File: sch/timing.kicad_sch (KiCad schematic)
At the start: 5 parts

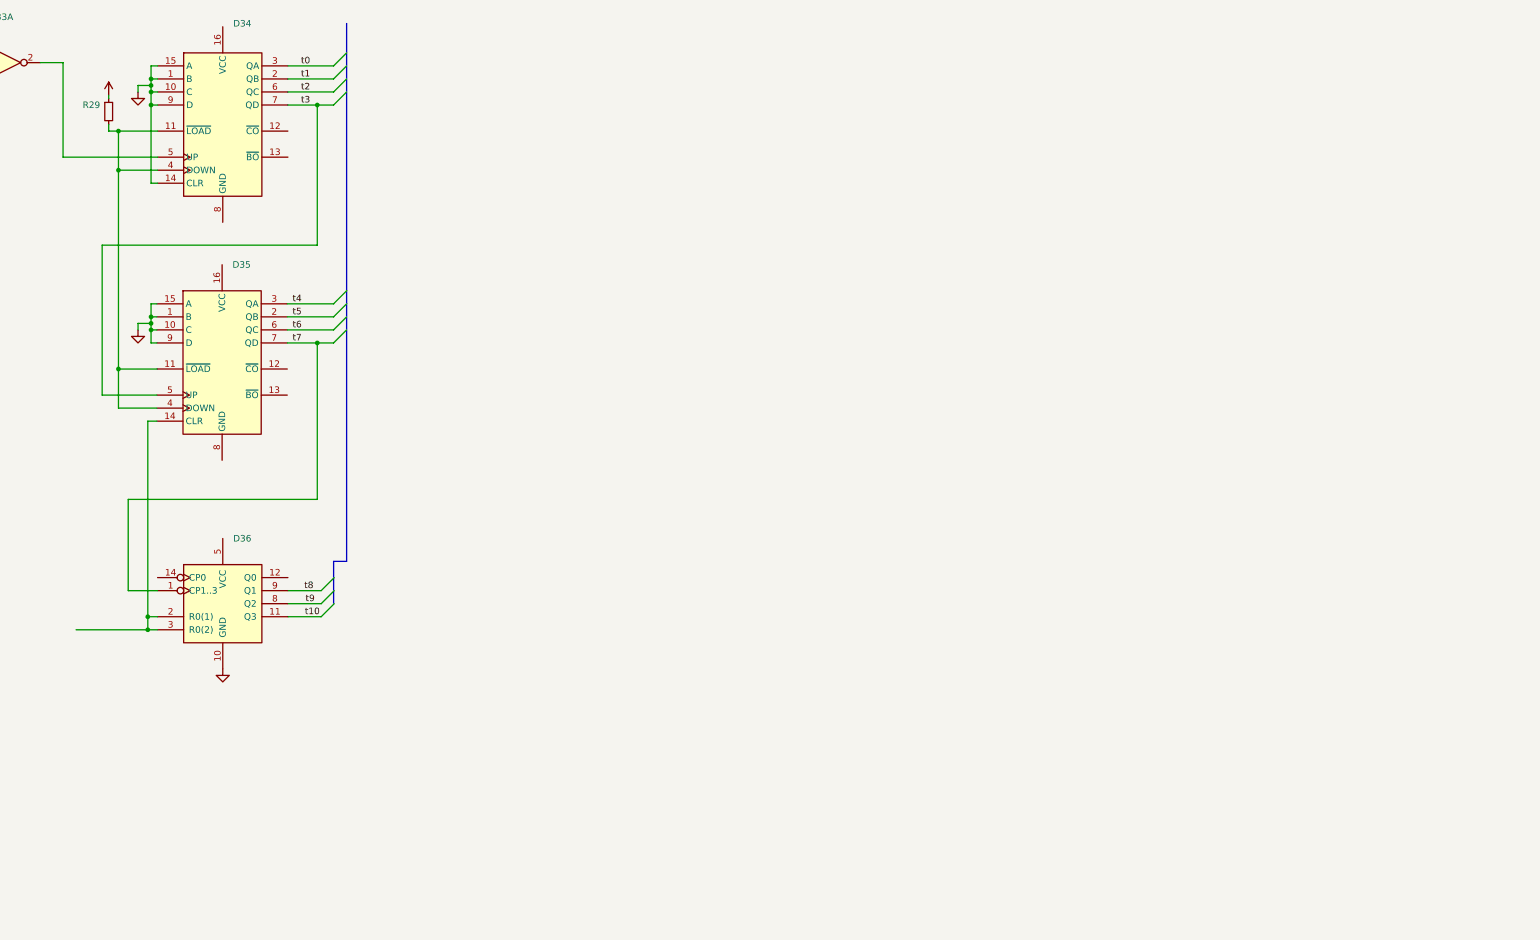
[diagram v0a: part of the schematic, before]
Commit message: Sch: timing sheet - added all elements
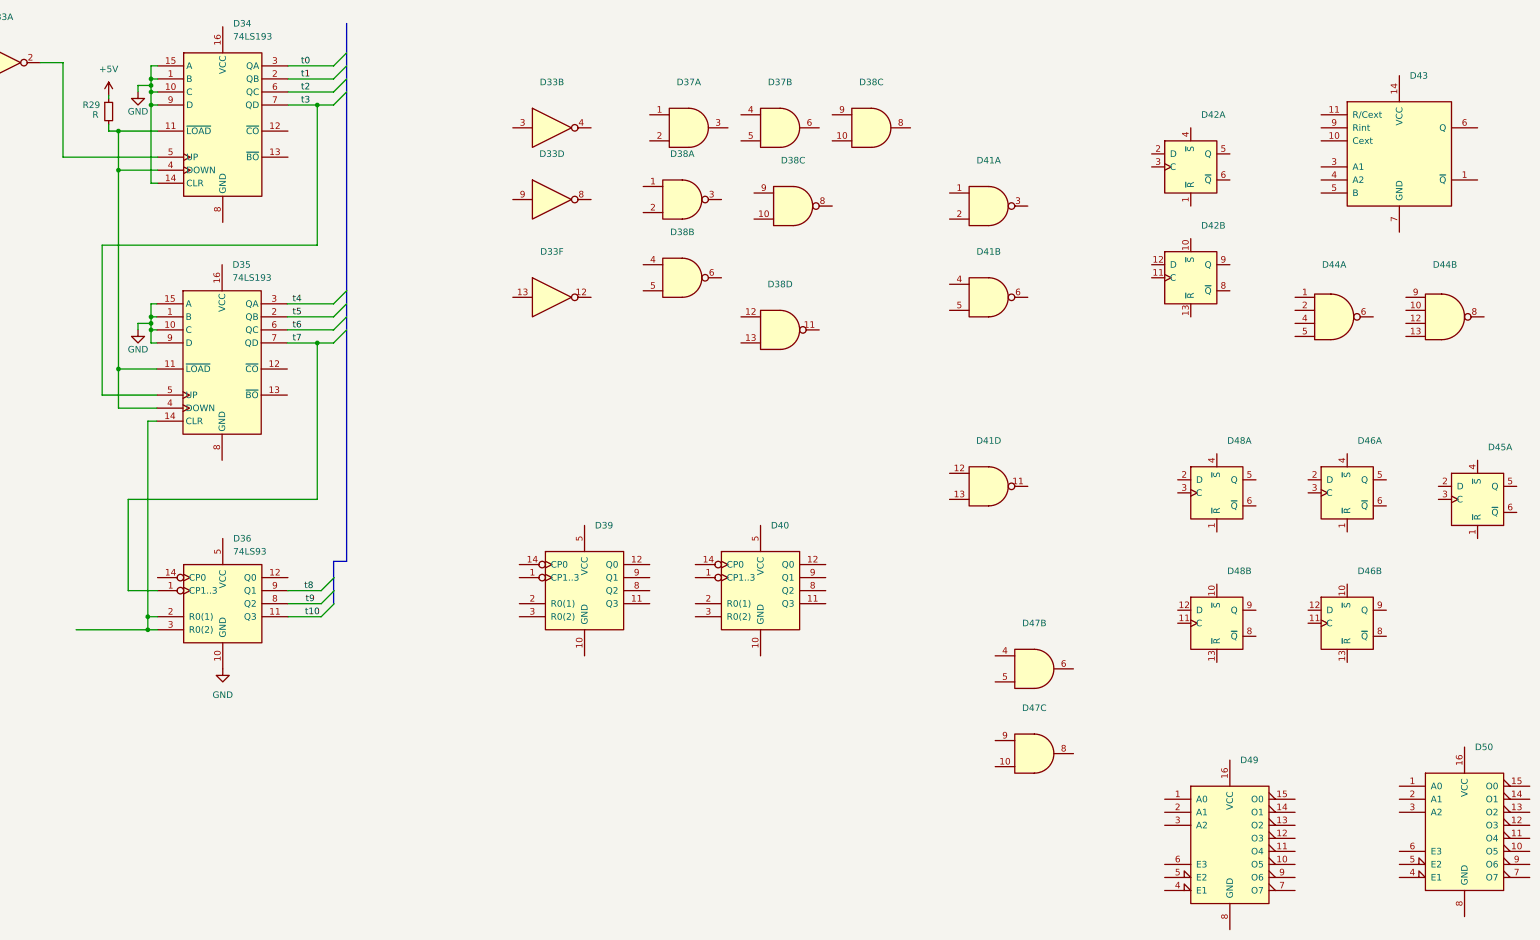
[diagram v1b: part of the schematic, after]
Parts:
- added unit 6 of D33
- added unit 2 of D33
- added unit 4 of D33
- added D37, D47: (no value), symbol 74xx:74LS08
- added D38, D41: (no value), symbol 74xx:74LS00
- added D39, D40: (no value), symbol 74xx:74LS93
- added D42, D45, D46, D48: (no value), symbol 74xx:74LS74
- added D43: (no value), symbol 74xx:74LS121
- added D44: (no value), symbol 74xx:74LS20
- added D49, D50: (no value), symbol 74xx:74LS138
- D34, D35: value (none) -> 74LS193
- D36: value (none) -> 74LS93
- R29: value (none) -> R

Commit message: SCH: timing block - work in progress
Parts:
- removed D43: (no value), symbol 74xx:74LS121
- added D1: (no value), symbol 74xx:74LS10
- added D18: (no value), symbol 74xx:74LS32
- added unit 4 of D37
- added D43: (no value), symbol 74xx:74LS123
- added R15, R16: (no value), symbol Device:R_Small
- D33: value (none) -> 74S04
- D38, D41: value (none) -> 74LS00
- D39, D40: value (none) -> 74LS93
- D42, D45, D46, D48: value (none) -> 74LS74
- D44: value (none) -> 74LS20
- D49, D50: value (none) -> 74LS138
- renumbered D38 to D37
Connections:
- net +5V: now also D49.16 (VCC), D50.16 (VCC), R15.1
- net GND: now also D46.11 (C), D46.12 (D), D46.2 (D), D46.3 (C), D48.11 (C), D48.12 (D), D48.2 (D), D48.3 (C), D49.8 (GND), D50.8 (GND)
- net t0: now also D37.4, D49.1 (A0), D50.1 (A0)
- net t1: now also D37.5, D49.2 (A1), D50.2 (A1)
- net t10: now also D37.10
- net t2: now also D49.3 (A2), D50.3 (A2)
- net t3: now also D33.3, D47.2, D50.6 (E3)
- net t6: now also D44.2
- net t7: now also D38.10, D38.9
- net t8: now also D38.1, D38.2
- net t9: now also D44.13
- net at D38.4: now also D43.4 (~{Q})
- net at D38.5: now also D45.1 (~{R}), D43.12 (~{Q})
- net CLK2: now reaches D38.6
- net CLK2: now also D35.14 (CLR), D36.2 (R0(1)), D36.3 (R0(2)), D39.14 (CP0)
- net at D41.11: now also D45.3 (C)
- net t18: now reaches D41.12
- net t18: now also D40.11 (Q3), D41.13
- net at D45.2 (D): now also D45.6 (~{Q})
- net at D45.5 (Q): now also D37.13
- net ~{KCU}: now reaches D41.4
- net ~{KCU}: now also D44.8
- net ~{CCU}: now reaches D41.5
- net ~{CCU}: now also D44.6
- net CSYNC: now reaches D41.6
- net RAM_RD_STB: now reaches D33.12
- net at D33.13: now also D50.9 (O6)
- net at D33.4: now also D37.2
- net t2??: now reaches D37.1
- net PIX_SR_LOAD: now reaches D37.3
- net at D44.10: now also D41.3
- net t15: now reaches D44.12
- net t15: now also D40.1 (CP1..3), D40.12 (Q0)
- net PIX_EN1: now reaches D44.9
- net PIX_EN1: now also D37.11, D43.9 (A)
- net at D33.8: now also D42.11 (C)
- net z5: now reaches D33.9
- net z5: now also D46.13 (~{R}), D49.9 (O6)
- net ~{RESIN}: now reaches D47.10
- net at D47.8: now also D50.4 (E1), D50.5 (E2)
- net ~{K1}: now reaches D47.9
- net ~{K1}: now also D42.8 (~{Q}), D47.1, D18.5
- net t16: now reaches D41.1
- net t16: now also D40.9 (Q1), D41.2
- net at D38.3: now also D37.9
- net z3: now reaches D48.10 (~{S})
- net z3: now also D49.12 (O3)
- net z6: now reaches D48.13 (~{R})
- net z6: now also D46.1 (~{R}), D49.7 (O7)
- net ~{CAS}: now reaches D48.8 (~{Q})
- net t14: now reaches D40.14 (CP0)
- net t14: now also D39.11 (Q3)
- net rst2: now reaches D40.2 (R0(1))
- net rst2: now also D39.2 (R0(1)), D39.3 (R0(2)), D40.3 (R0(2)), D43.5 (Q)
- net t17: now reaches D40.8 (Q2)
- net t17: now also D38.12, D38.13
- net at D42.10 (~{S}): now also D42.1 (~{R}), R16.2
- net at D42.12 (D): now also D42.6 (~{Q})
- net VIDEO-CPU: now reaches D42.13 (~{R})
- net VIDEO-CPU: now also D42.4 (~{S}), D50.7 (O7)
- net K1: now reaches D42.9 (Q)
- net at D49.10 (O5): now also D48.1 (~{R})
- net z2: now reaches D49.13 (O2)
- net z2: now also D46.4 (~{S}), D48.4 (~{S})
- net z1: now reaches D49.14 (O1)
- net z1: now also D46.10 (~{S})
- net at D49.4 (E1): now also D47.3, D49.5 (E2)
- net at D49.6 (E3): now also R15.2
- net at D38.8: now also D44.4, D44.5
- net at D38.11: now also D37.12
- net 0_ROMSEL: now reaches D42.2 (D)
- net at D42.3 (C): now also D1.8
- net ~{RAS}: now reaches D46.8 (~{Q})
- net PIX_SR_CLK: now reaches D37.6
- net K0: now reaches D46.5 (Q)
- net t11: now reaches D39.1 (CP1..3)
- net t11: now also D39.12 (Q0)
- net t13: now reaches D39.8 (Q2)
- net t12: now reaches D39.9 (Q1)
- net at D37.8: now also D43.1 (A)
- new net: D18.3, D18.4
- new net ~{MEMR}: D1.9
- new net ~{MEMW}: D1.10, D1.11, D18.1
- new net ~{WE}: D18.6
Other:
- moved on the sheet: D33B, D33D, D33F, D37A, D37B, D37C, D38A, D38B, D38C, D38D, D39, D40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

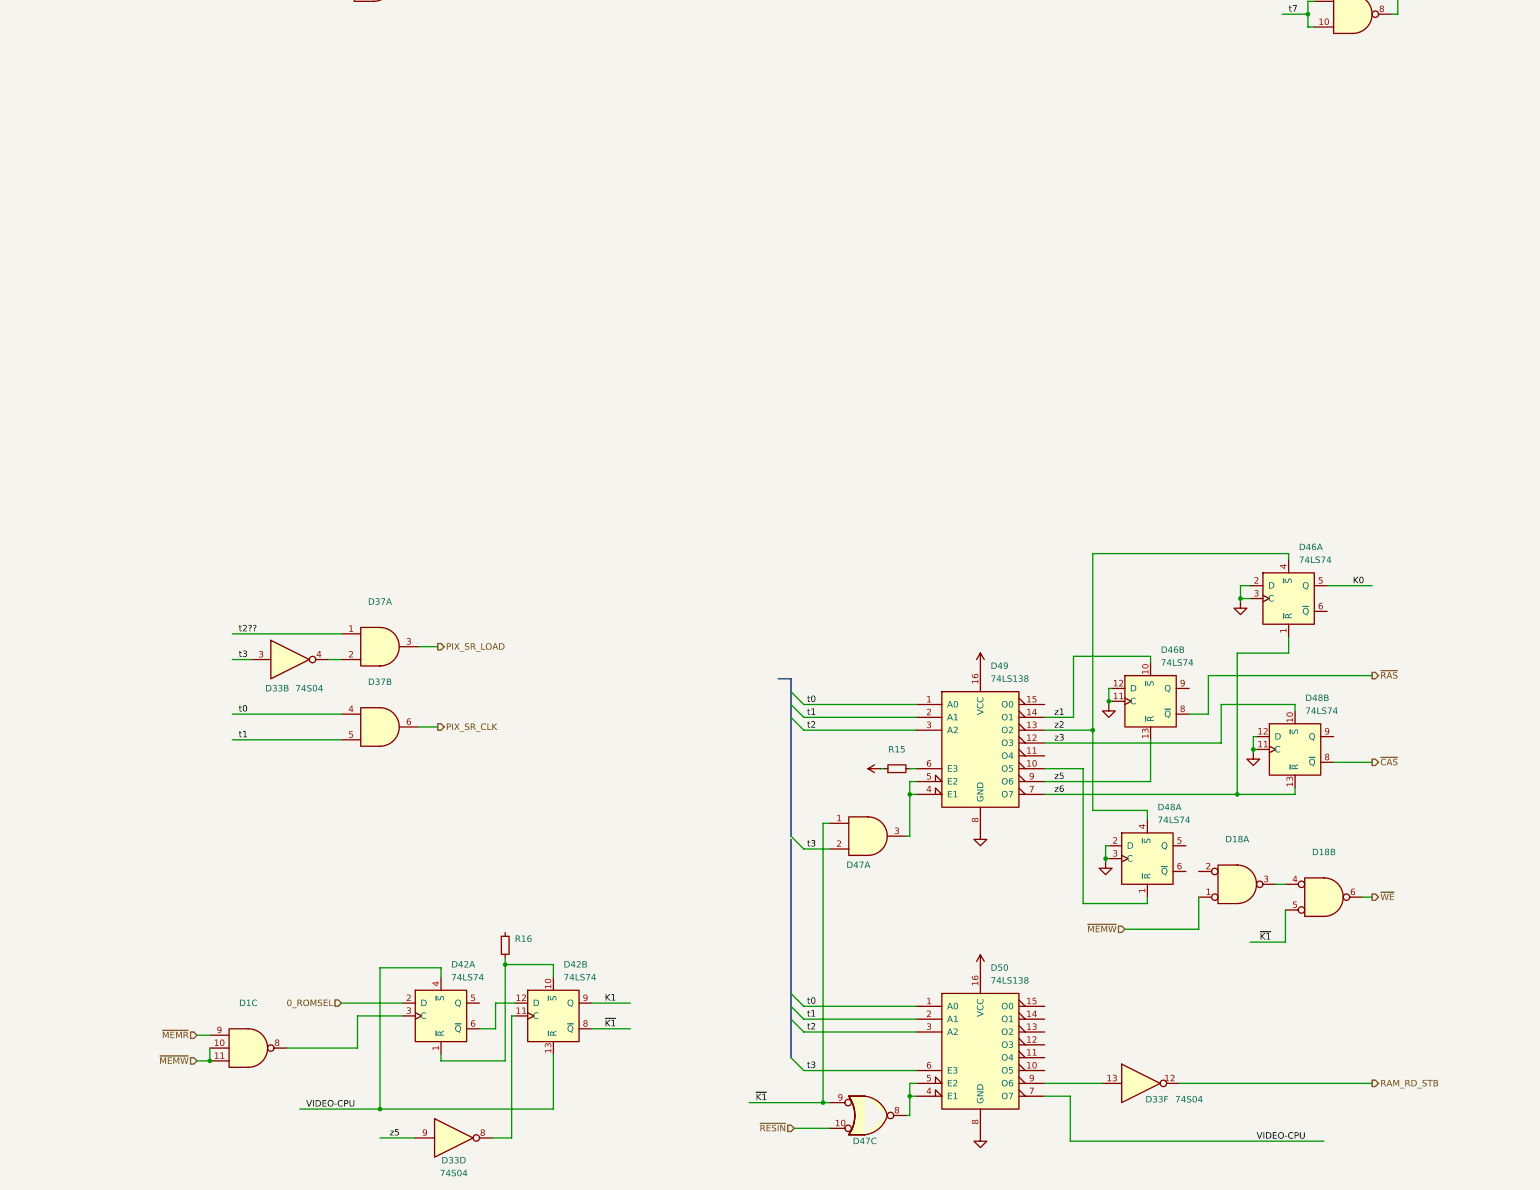
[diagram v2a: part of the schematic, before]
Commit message: Extracted RAM controller
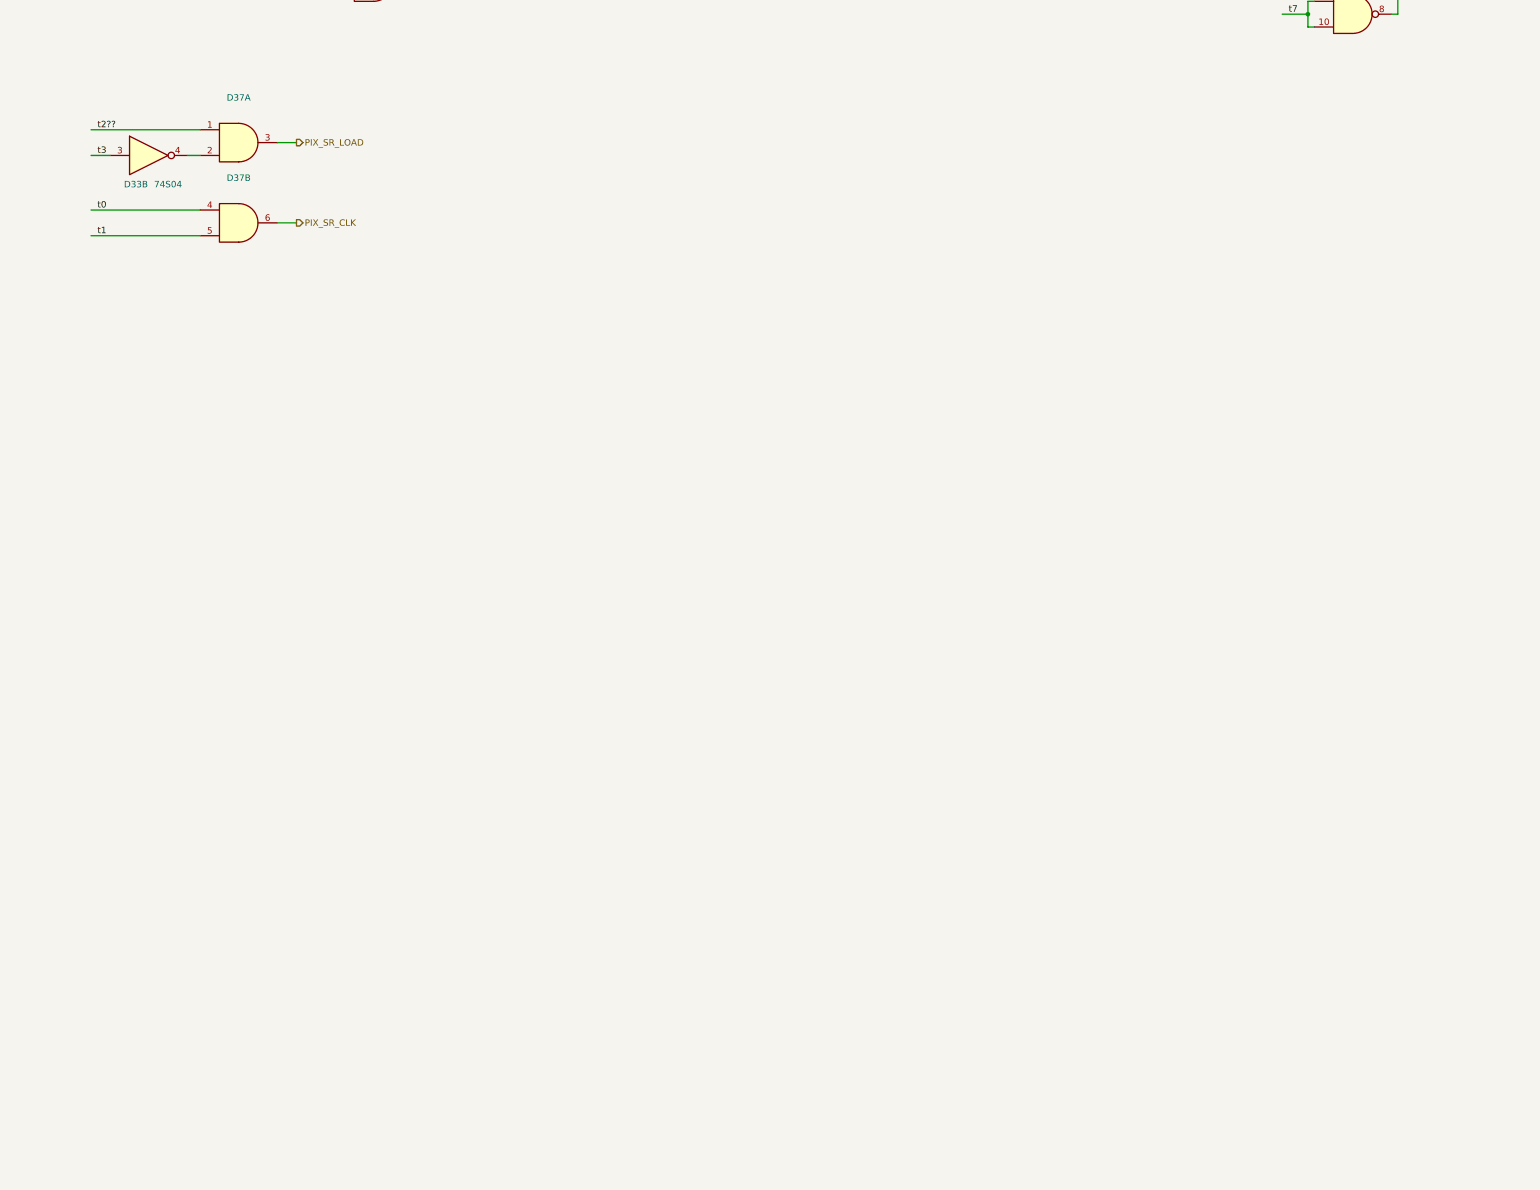
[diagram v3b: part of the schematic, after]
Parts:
- removed D1: (no value), symbol 74xx:74LS10
- removed D18: (no value), symbol 74xx:74LS32
- removed unit 6 of D33
- removed unit 4 of D33
- removed D42, D46, D48: 74LS74, symbol 74xx:74LS74
- removed D47: (no value), symbol 74xx:74LS08
- removed D49, D50: 74LS138, symbol 74xx:74LS138
- removed R15, R16: (no value), symbol Device:R_Small
- D37, D43: value (none) -> ~
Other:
- moved on the sheet: D33B, D37A, D37B

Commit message: Sch: timing counters block completed
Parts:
- removed unit 2 of D33
- removed unit 1 of D37
- removed unit 2 of D37
- removed unit 3 of D38
- removed unit 2 of D41
- removed unit 1 of D41
- removed D44: 74LS20, symbol 74xx:74LS20
- added C50: C_Small, symbol Device:C_Small
- added C51: ~, symbol Device:C_Small
- added R11, R13, R17: R_Small, symbol Device:R_Small
- added R12: ~, symbol Device:R_Small
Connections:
- net +5V: now also D34.16 (VCC), D35.16 (VCC), D36.5 (VCC), D39.5 (VCC), D40.5 (VCC), R11.1, R12.1, R13.2, R17.1
- net GND: now also D34.8 (GND), D35.8 (GND), D39.10 (GND), D40.10 (GND)
- net t19: now reaches D37.13, D45.5 (Q)
- net t_rst1: now reaches D37.8, D43.1 (A)
- net at D43.14 (Cext): now also C50.1
- net at D43.15 (RCext): now also C50.2, R11.2
- net at D43.2 (B): now also D43.10 (B), D43.11 (Clr), D43.3 (Clr), R17.2
- net at D45.4 (~{S}): now also R13.1
- net at D43.6 (Cext): now also C51.1
- net at D43.7 (RCext): now also C51.2, R12.2
- net CLK2: no longer names the net of D35.14 (CLR), D36.2 (R0(1)), D36.3 (R0(2)), D38.6, D39.14 (CP0)
- net PIX_EN1 renamed t_rst2
- net rst2: no longer names the net of D39.2 (R0(1)), D39.3 (R0(2)), D40.2 (R0(1)), D40.3 (R0(2)), D43.5 (Q)
- no-connect marks 0 -> 1
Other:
- note added: "mod16 counter"
- note added: "mod20 counter"
- note added: "mod320 counter"
- moved on the sheet: D33A, D34, D35, D36, D37C, D37D, D38A, D38B, D38D, D39, D40, D41D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

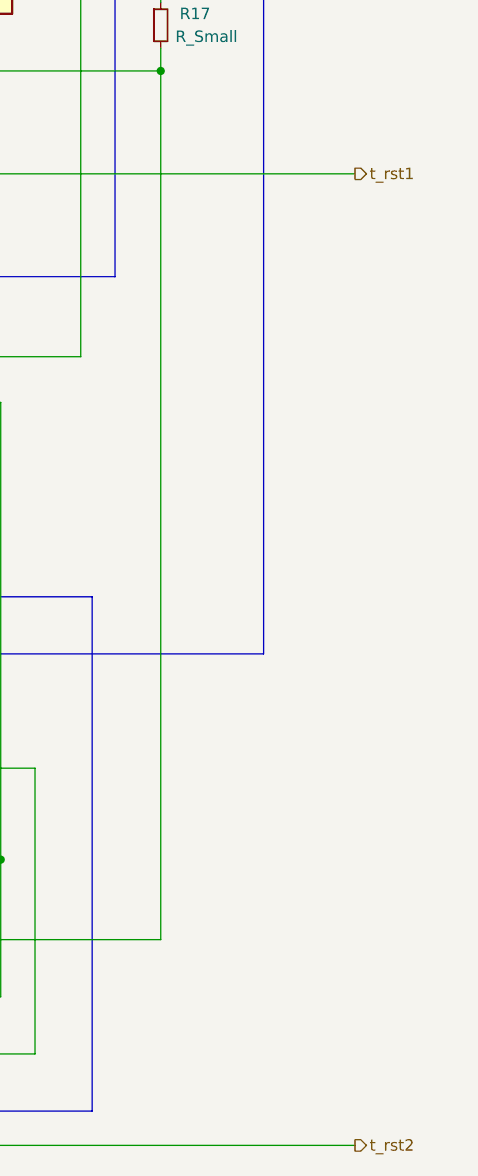
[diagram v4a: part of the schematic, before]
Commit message: Sch: mem remapping circuit moved to ROM sheet
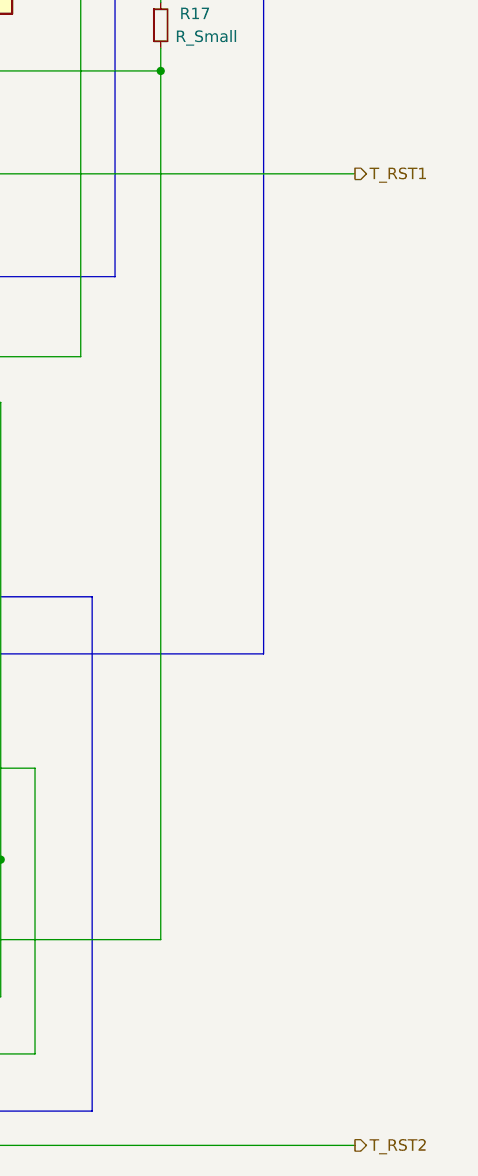
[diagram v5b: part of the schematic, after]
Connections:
- net t_rst1 renamed T_RST1
- net t_rst2 renamed T_RST2
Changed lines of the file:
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@@
     (effects (font (size 1.27 1.27)) (justify left bottom))
   )
-  (hierarchical_label "t_rst2" (shape output) (at 334.645 187.325 0)
+  (hierarchical_label "T_RST2" (shape output) (at 334.645 187.325 0)
     (effects (font (size 1.27 1.27)) (justify left))
   )
-  (hierarchical_label "t_rst1" (shape output) (at 334.645 79.375 0)
+  (hierarchical_label "T_RST1" (shape output) (at 334.645 79.375 0)
     (effects (font (size 1.27 1.27)) (justify left))
   )
